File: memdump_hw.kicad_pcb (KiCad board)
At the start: 2 copper layers, 56.1 x 86.1 mm, 76 parts, among them J1 USB_C_USB2.0, J2 SWD, J3 LEVEL, J4 BOOT0, Q1 SI4800, SW1 RESET, U1 AMS1117-3.3, U2 STM32F103C8, U3 74HC595, U4 74HC595, U5 74HC595, U6 SST39SF040, Y1 12M

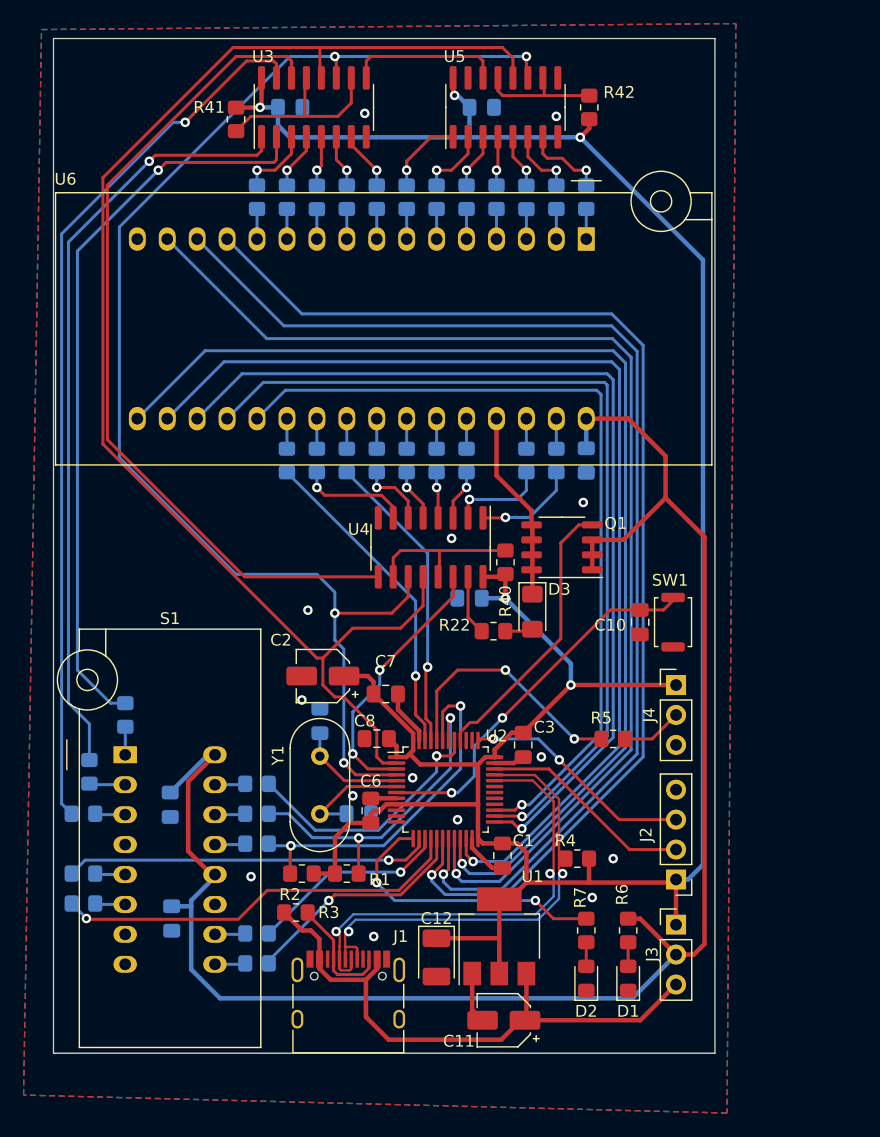
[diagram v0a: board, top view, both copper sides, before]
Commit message: fix: minor cleanup fix: branching from vias when possible fix: values moved to the respective silkscreens
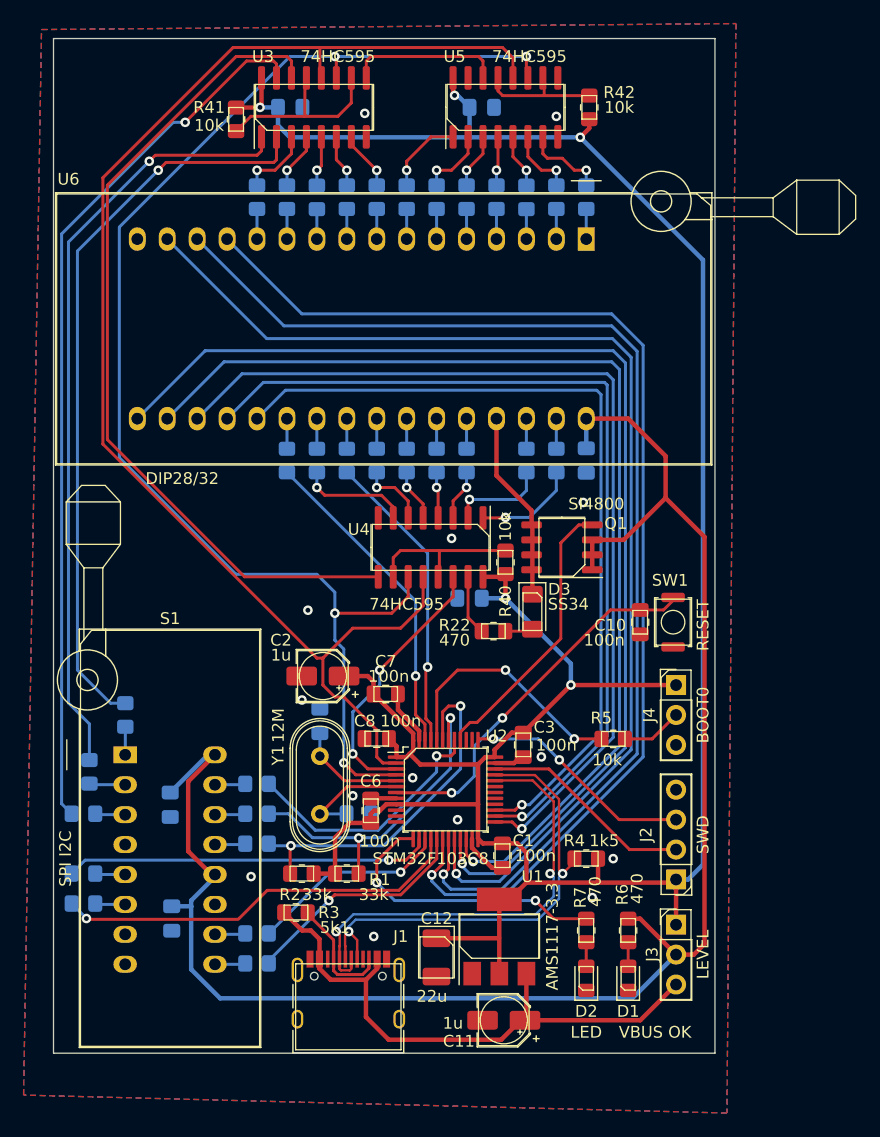
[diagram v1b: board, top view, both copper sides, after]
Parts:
- S1: value MEMSOCKET -> SPI I2C
- U6: value SST39SF040 -> DIP28/32
- moved R4 0.76 mm to (213.9, 126.2)
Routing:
- net GND: track 17.6 -> 13.1 mm
- net USB_D+: track 38.6 -> 40.8 mm
